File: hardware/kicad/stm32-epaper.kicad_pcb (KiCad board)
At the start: 4 copper layers, 97.4 x 60 mm, 156 parts, among them J1 USB_C_Receptacle_USB2.0_16P, J101 TC2050-IDC-NL, J102 UART (TX RX GND), J2 BATT (1S LiPo), J201 microSD, J301 IT8951 HAT, J302 Electrodes L, J303 Electrodes R, SW101 BOOT, SW301 PEC11R-4220F-S0024, SW302 POWER, U1 BQ24073RGT, U101 STM32F469IIT6, U2 TPS63802DLA, U201 IS42S16400J-6TLI, U202 W25Q128JVSIQ, U3 TPS61023DRL, U301 CAP1188-1-CP-TR, U302 TPD2E2U06DCKR, U303 TPD2E2U06DCKR, U4 TPS22965DSG, U5 USBLC6-2SC6, U6 TPS63900DSK, U7 MCP1700T-3002E/TT, Y101 8MHz CL8pF, Y102 32.768kHz CL6pF

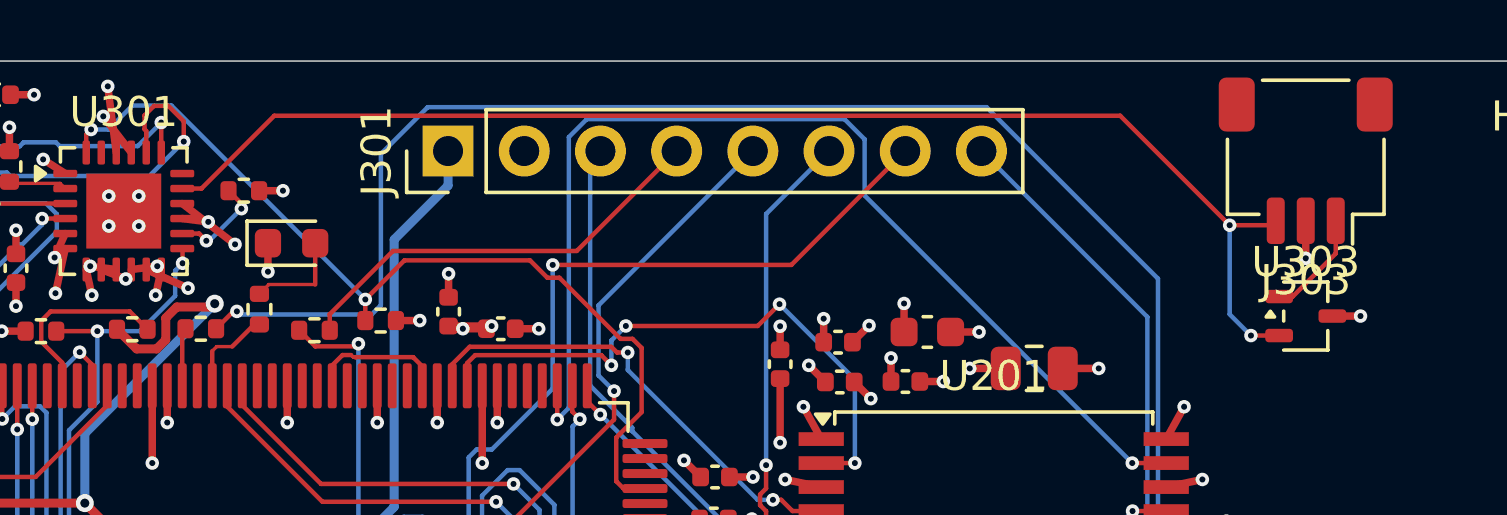
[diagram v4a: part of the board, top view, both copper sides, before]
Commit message: Last-mile: keep-out aware, --direct mode; CAP1188 corridor narrowed to the touch pins
attempt 13 + last-mile: 2 unconnected (CAP1188 VDD-C301, one GND stub).

Co-Authored-By: Claude Opus 5.5 <noreply@anthropic.com>
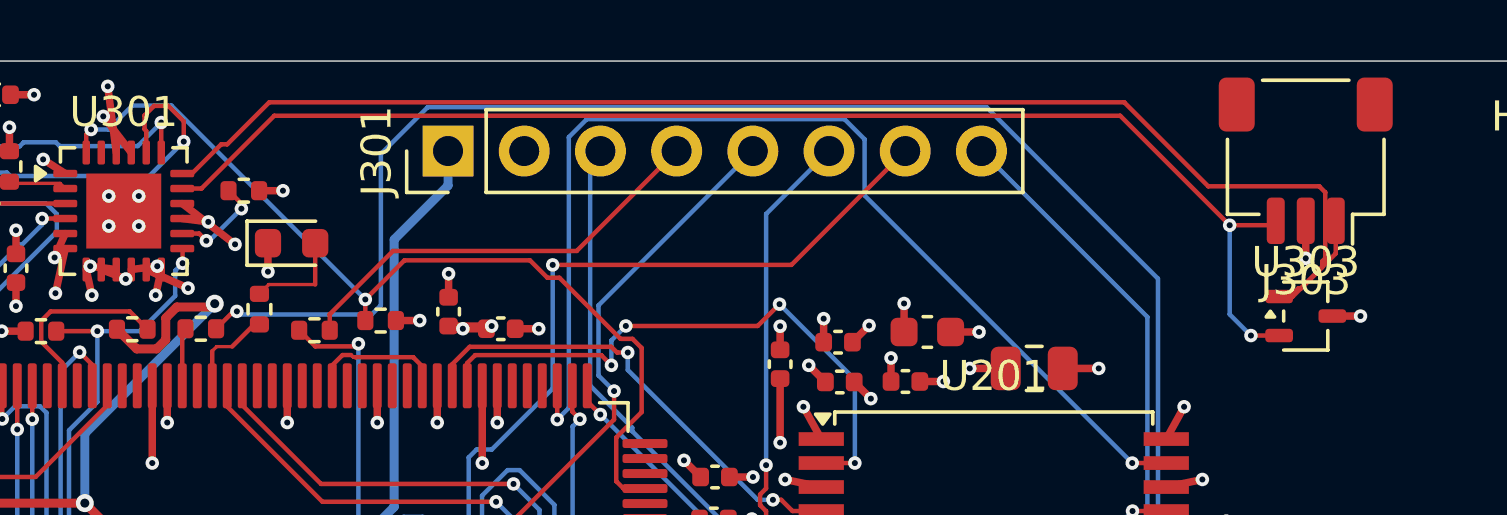
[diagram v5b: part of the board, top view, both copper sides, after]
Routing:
- net /Peripherals/TOUCH_R1: track 3.57 -> 48.3 mm
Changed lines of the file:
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@@
+	)
+	(segment
+		(start 182.649999 107.875)
+		(end 182.5125 107.85)
+		(width 0.15)
+		(layer "F.Cu")
+		(net "/Peripherals/TOUCH_R1")
+	)
+	(segment
+		(start 184.049999 104.375)
+		(end 184.049999 106.574999)
+		(width 0.15)
+		(layer "F.Cu")
+		(net "/Peripherals/TOUCH_R1")
+	)
+	(segment
+		(start 183.95 106.875)
+		(end 183.25 107.574999)
+		(width 0.15)
+		(layer "F.Cu")
+		(net "/Peripherals/TOUCH_R1")
+	)
+	(segment
+		(start 184.049999 106.574999)
+		(end 183.95 106.675)
+		(width 0.15)
+		(layer "F.Cu")
+		(net "/Peripherals/TOUCH_R1")
+	)
+	(segment
+		(start 145.95 103.75)
+		(end 146.049999 103.774999)
+		(width 0.15)
+		(layer "F.Cu")
+		(net "/Peripherals/TOUCH_R1")
 	)
 	(segment
 		(start 182.5125 107.85)
 		(end 182.9652 107.85)
+		(width 0.15)
+		(layer "F.Cu")
+		(net "/Peripherals/TOUCH_R1")
+	)
+	(segment
+		(start 183.049999 107.675)
+		(end 182.95 107.675)
+		(width 0.15)
+		(layer "F.Cu")
+		(net "/Peripherals/TOUCH_R1")
+	)
+	(segment
+		(start 182.95 107.675)
+		(end 182.85 107.774999)
+		(width 0.15)
+		(layer "F.Cu")
+		(net "/Peripherals/TOUCH_R1")
+	)
+	(segment
+		(start 183.25 107.574999)
+		(end 183.149999 107.574999)
+		(width 0.15)
+		(layer "F.Cu")
+		(net "/Peripherals/TOUCH_R1")
+	)
+	(segment
+		(start 180.149999 104.175)
+		(end 183.85 104.175)
+		(width 0.15)
+		(layer "F.Cu")
+		(net "/Peripherals/TOUCH_R1")
+	)
+	(segment
+		(start 183.85 104.175)
+		(end 184.049999 104.375)
+		(width 0.15)
+		(layer "F.Cu")
+		(net "/Peripherals/TOUCH_R1")
+	)
+	(segment
+		(start 146.25 103.774999)
+		(end 147.25 102.774999)
+		(width 0.15)
+		(layer "F.Cu")
+		(net "/Peripherals/TOUCH_R1")
+	)
+	(segment
+		(start 147.45 102.774999)
+		(end 148.85 101.375)
 		(width 0.15)
 		(layer "F.Cu")
@@
 	)
 	(segment
+		(start 183.149999 107.574999)
+		(end 183.049999 107.675)
+		(width 0.15)
+		(layer "F.Cu")
+		(net "/Peripherals/TOUCH_R1")
+	)
+	(segment
 		(start 182.9652 107.85)
 		(end 184.4 106.4152)
 		(width 0.15)
 		(layer "F.Cu")
+		(net "/Peripherals/TOUCH_R1")
+	)
+	(segment
+		(start 146.049999 103.774999)
+		(end 146.25 103.774999)
+		(width 0.15)
+		(layer "F.Cu")
+		(net "/Peripherals/TOUCH_R1")
+	)
+	(segment
+		(start 177.35 101.375)
+		(end 180.149999 104.175)
+		(width 0.15)
+		(layer "F.Cu")
+		(net "/Peripherals/TOUCH_R1")
+	)
+	(segment
+		(start 147.25 102.774999)
+		(end 147.45 102.774999)
+		(width 0.15)
+		(layer "F.Cu")
+		(net "/Peripherals/TOUCH_R1")
+	)
+	(segment
+		(start 183.95 106.675)
+		(end 183.95 106.875)
+		(width 0.15)
+		(layer "F.Cu")
+		(net "/Peripherals/TOUCH_R1")
+	)
+	(segment
+		(start 182.75 107.774999)
+		(end 182.649999 107.875)
+		(width 0.15)
+		(layer "F.Cu")
+		(net "/Peripherals/TOUCH_R1")
+	)
+	(segment
+		(start 148.85 101.375)
+		(end 177.35 101.375)
+		(width 0.15)
+		(layer "F.Cu")
+		(net "/Peripherals/TOUCH_R1")
+	)
+	(segment
+		(start 182.85 107.774999)
+		(end 182.75 107.774999)
+		(width 0.15)
+		(layer "F.Cu")

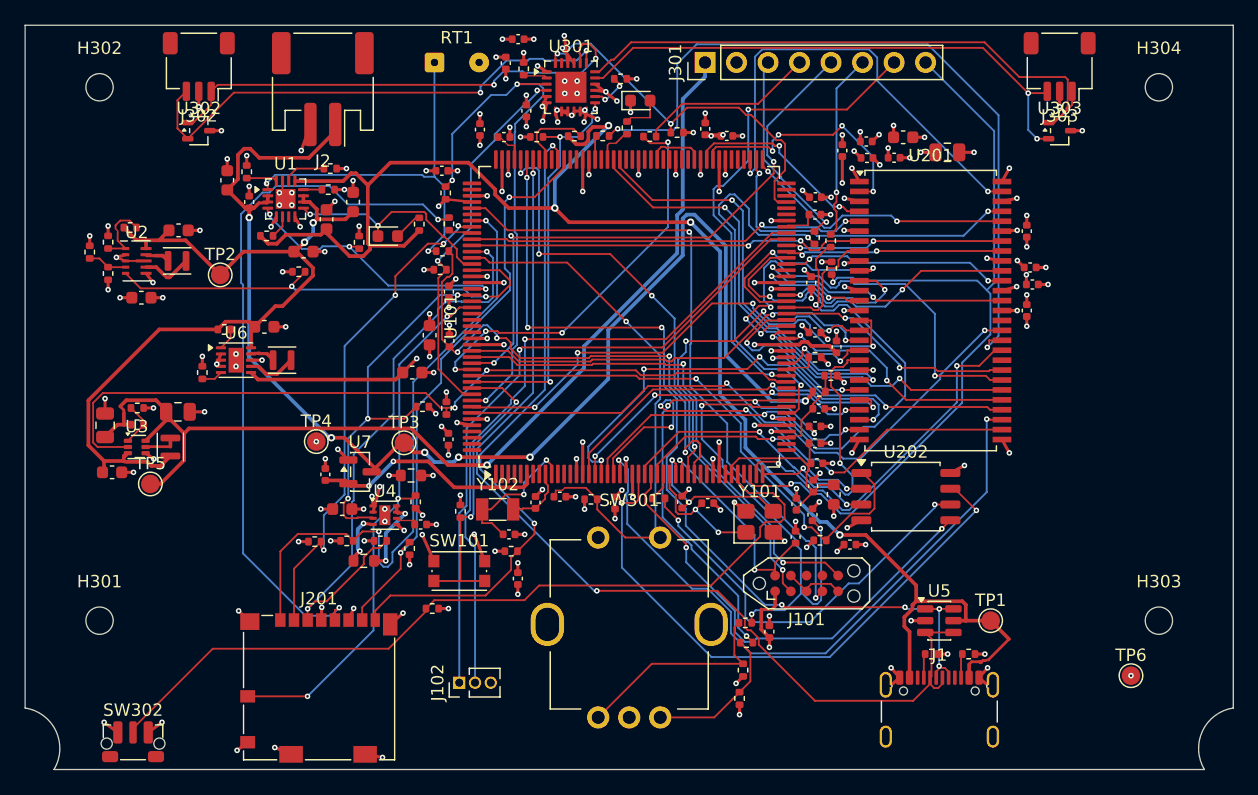
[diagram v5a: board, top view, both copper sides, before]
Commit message: attempt 14 + last-mile: 2 unconnected, 48 DRC errors; keep-out rules split; U6 over 3V3_AON; wider last-mile retry
Co-Authored-By: Claude Opus 5.5 <noreply@anthropic.com>
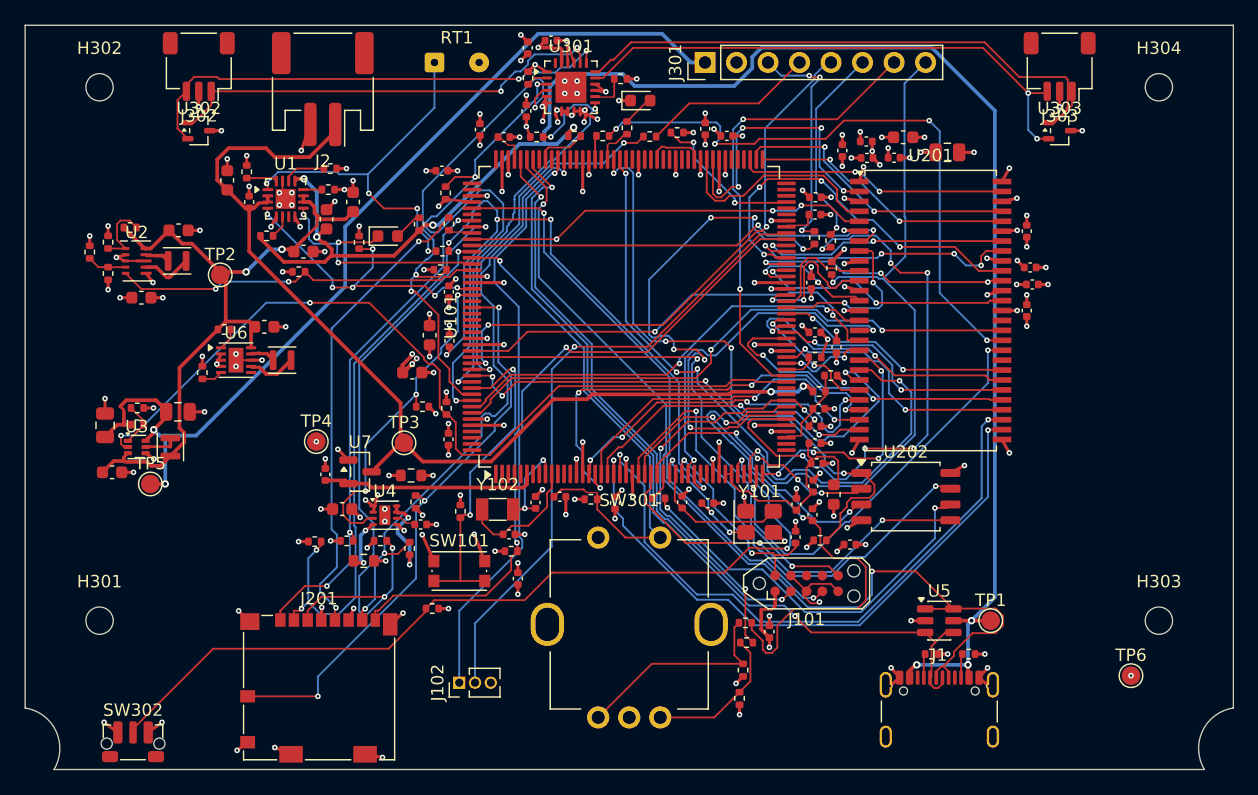
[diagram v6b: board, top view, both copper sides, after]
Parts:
- moved C301 2.66 mm to (142.4, 101.2)
- moved C302 2.16 mm to (140.5, 101.8)
- moved R308 0.82 mm to (140.6, 104.2)
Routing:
- net +BATT: track 104.7 -> 82.8 mm, vias 6 -> 2
- net FMC_BA0: track 33.3 -> 53.9 mm, vias 2 -> 4
- net SDCARD_CLK: track 57.6 -> 38.1 mm
- net CAP_RESET: track 30.5 -> 12.6 mm
- net FMC_D15: track 36.7 -> 21.8 mm
- net FMC_BA1: track 33.7 -> 48.0 mm, vias 2 -> 4
- net EPD_CS: track 32.3 -> 46.4 mm, vias 2 -> 6
- net FMC_A9: track 36.7 -> 23.3 mm, vias 4 -> 2
- net USB_DM: track 81.0 -> 68.4 mm
- net VSYS: track 67.1 -> 55.1 mm
- net TS_SENSE: track 41.8 -> 53.3 mm, vias 4 -> 5
- net SPI1_SCK: track 31.8 -> 43.2 mm, vias 2 -> 6
- net EPD_HRDY: track 67.4 -> 56.6 mm
- net SDRAM_CLK: track 60.6 -> 50.0 mm, vias 2 -> 4
- net I2C1_SCL: track 30.7 -> 40.8 mm, vias 2 -> 3
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
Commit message: Routing attempt 15 + last-mile: 2 unconnected (both at CAP1188 pins), 48 DRC errors
U6 moved over the 3V3_AON plane; USB pair and QSPI rules now pass; 4
narrow power tracks left. Remaining gaps always cluster at the CAP1188.

Co-Authored-By: Claude Opus 5.5 <noreply@anthropic.com>
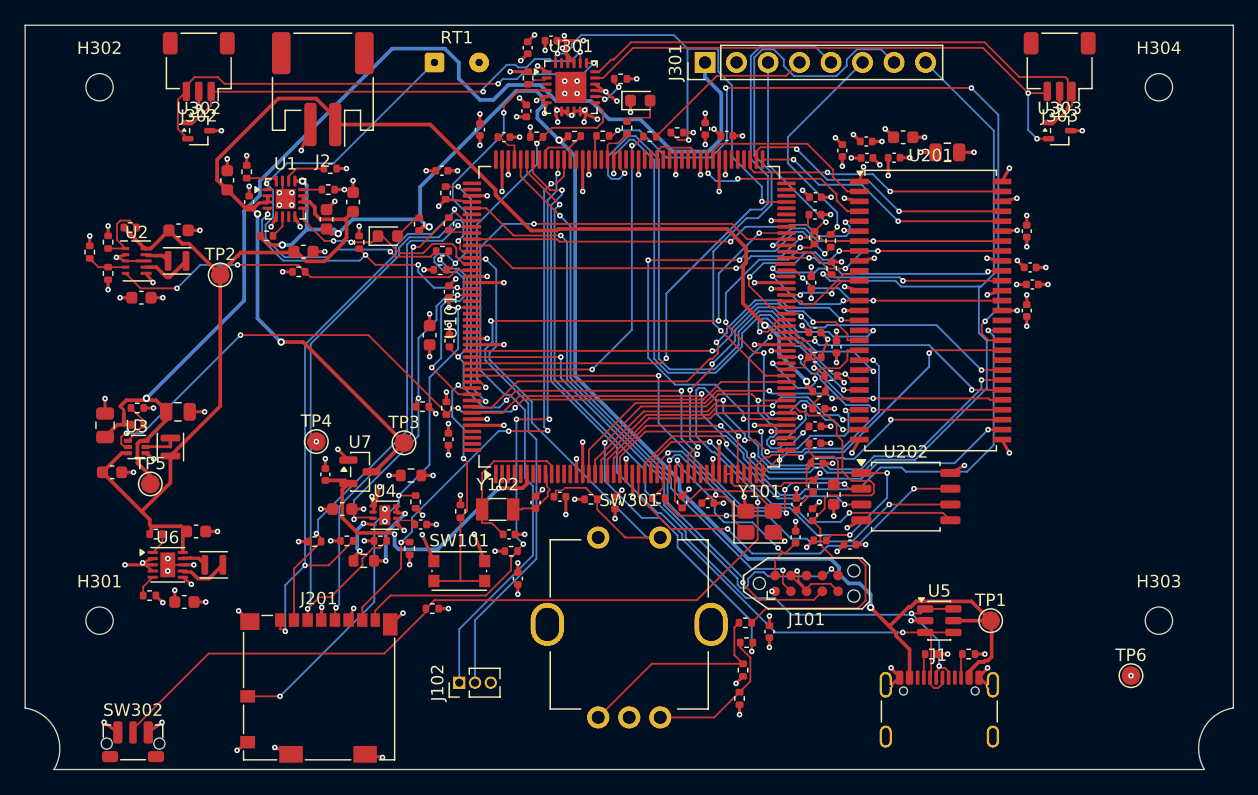
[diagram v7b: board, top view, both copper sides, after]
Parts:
- moved C7 26.1 mm to (112.8, 146.5)
- moved R16 18.5 mm to (110.0, 146.0), turned to 0 degrees
- moved L3 17.4 mm to (115.2, 143.5)
- moved U6 17.4 mm to (111.5, 143.5)
- moved C6 17.4 mm to (113.8, 140.8)
- moved R17 17.4 mm to (110.5, 141.0)
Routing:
- net CAP_RESET: track 12.6 -> 39.8 mm, vias 2 -> 3
- net I2C1_SDA: track 46.1 -> 20.4 mm, vias 3 -> 2
- net VBUS: track 141.3 -> 121.0 mm, vias 7 -> 6
- net SPI1_SCK: track 43.2 -> 24.5 mm, vias 6 -> 4
- net +BATT: track 82.8 -> 100.4 mm, vias 2 -> 4
- net ENC_B: track 34.5 -> 48.7 mm
- net FMC_A5: track 51.1 -> 37.0 mm
- net FMC_D10: track 31.2 -> 18.0 mm, vias 4 -> 2
- net /MCU/USART3_TX: track 52.5 -> 65.5 mm
- net FMC_A4: track 50.2 -> 37.3 mm
- net TS_SENSE: track 53.3 -> 40.4 mm
- net FMC_A9: track 23.3 -> 36.2 mm
- net +5V: track 78.4 -> 91.3 mm, vias 2 -> 1
- net FMC_NBL1: track 47.7 -> 59.8 mm
- net VSYS: track 55.1 -> 66.1 mm, vias 2 -> 0
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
